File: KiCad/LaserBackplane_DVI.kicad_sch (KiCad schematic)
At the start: 48 parts, among them J1 Curr. Mod., J2 DVI-I, J5 Pz+, J6 Pz-, J7 Piezo_In, J8 Conn_Coaxial, K1 G6AU, Q1 MMBT3904, Q2 2N4401, U1 ADA4807-2ARM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

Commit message: Do not place the LED for assembly as this needs to match the frontpanel mounting hole (#15)
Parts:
- D4: Config (none) -> -PCBA
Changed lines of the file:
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@@
+			)
+		)
+		(property "Config" "-PCBA"
+			(at 165.1 41.91 90)
+			(effects
+				(font
+					(size 1.27 1.27)
+				)
+				(hide yes)
 			)
 		)

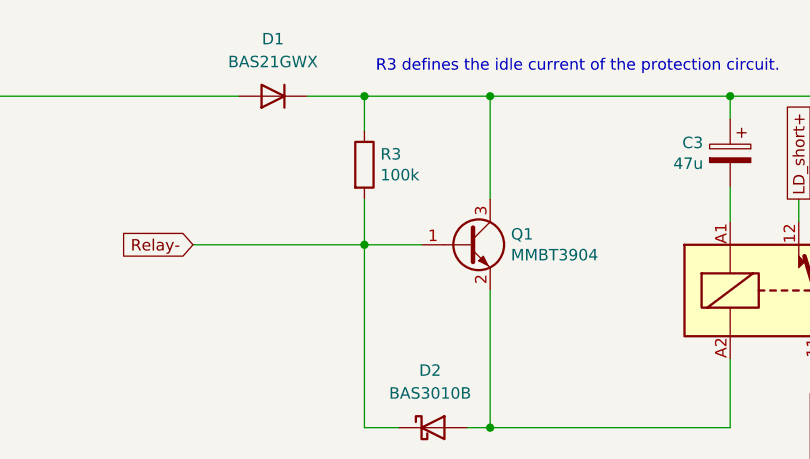
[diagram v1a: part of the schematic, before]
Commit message: Change R3 from 100k to 47k to increase the current through the relay during switch off
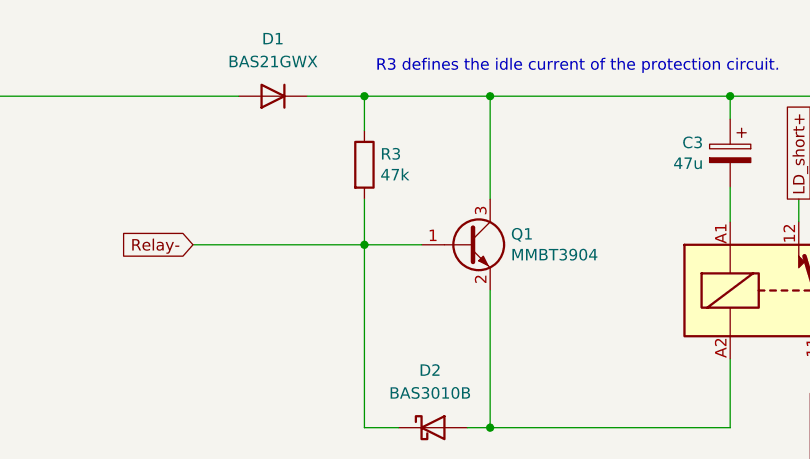
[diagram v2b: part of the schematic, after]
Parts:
- R3: value 100k -> 47k; PN CRCW0603100KFKEA -> CRCW060347K0FKEA
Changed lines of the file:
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@@
 			)
 		)
-		(property "Value" "100k"
+		(property "Value" "47k"
 			(at 85.598 32.893 0)
 			(effects
@@
 			)
 		)
-		(property "PN" "CRCW0603100KFKEA"
+		(property "PN" "CRCW060347K0FKEA"
 			(at 83.82 31.75 0)
 			(effects

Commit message: Bump to 1.8.1 (#17)
Updated authors
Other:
- company: Atoms-Photons-Quanta, Institut für Angewandte Physik, TU Darmstadt -> Atoms-Photons-Quanta, TU Darmstadt and Quantum Electronic Devices GmbH
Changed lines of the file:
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@@
 	(title_block
 		(title "Laser Backplane Diode DVI")
-		(date "2025-06-24")
-		(rev "1.8.0")
-		(company "Atoms-Photons-Quanta, Institut für Angewandte Physik, TU Darmstadt")
+		(date "2025-06-27")
+		(rev "1.8.1")
+		(company "Atoms-Photons-Quanta, TU Darmstadt and Quantum Electronic Devices GmbH")
 		(comment 1 "and Tilman Preuschoff")
-		(comment 2 "Copyright (©) 2024, Patrick Baus <patrick.baus@physik.tu-darmstadt.de>")
+		(comment 2 "Copyright (©) 2025, Patrick Baus <patrick.baus@quantum-electronic-devices.de>")
 	)
 	(text "R3 defines the idle current of the protection circuit."
@@
 	(symbol
 		(lib_id "Graphic:Logo_Open_Hardware_Small")
-		(at 275.59 173.99 0)
+		(at 279.4 176.53 0)
 		(unit 1)
 		(exclude_from_sim no)
@@
 		(dnp no)
 		(property "Reference" "LOGO2"
-			(at 275.59 167.005 0)
+			(at 279.4 169.545 0)
 			(effects
 				(font
@@
 		)
 		(property "Value" "Logo_Open_Hardware_Small"
-			(at 275.59 179.705 0)
+			(at 279.4 182.245 0)
 			(effects
 				(font
@@
 		)
 		(property "Footprint" "Symbol:OSHW-Logo_7.5x8mm_SilkScreen"
-			(at 275.59 173.99 0)
+			(at 279.4 176.53 0)
 			(effects
 				(font
@@
 		)
 		(property "Datasheet" "~"
-			(at 275.59 173.99 0)
+			(at 279.4 176.53 0)
 			(effects
 				(font
@@
 		)
 		(property "Description" "Open Hardware logo, small"
-			(at 275.59 173.99 0)
+			(at 279.4 176.53 0)
 			(effects
 				(font
@@
 		)
 		(property "MFN" ""
-			(at 275.59 173.99 0)
+			(at 279.4 176.53 0)
 			(effects
 				(font
@@
 		)
 		(property "PN" ""
-			(at 275.59 173.99 0)
+			(at 279.4 176.53 0)
 			(effects
 				(font

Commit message: Do not place the current mod SMA when using the PCBA service.
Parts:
- J1: Config +curr_mod -> +curr_mod,-PCBA
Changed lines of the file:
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@@
 			)
 		)
-		(property "Config" "+curr_mod"
+		(property "Config" "+curr_mod,-PCBA"
 			(at 25.4 161.29 0)
 			(effects

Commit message: Fixed product number of the relay. Removed dash before DC9 at the end.
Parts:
- K1: PN G6AU-274P-ST-US-DC9 -> G6AU-274P-ST-US DC9
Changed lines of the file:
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@@
 			)
 		)
-		(property "PN" "G6AU-274P-ST-US-DC9"
+		(property "PN" "G6AU-274P-ST-US DC9"
 			(at 134.62 45.72 0)
 			(effects

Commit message: Updared EEPROM symbol Enabled more ERC rules
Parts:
- U4: symbol Microchip:AT21CS11-STXXXX-X -> Microchip:AT21CS11-STU10‑T
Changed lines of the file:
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@@
 	)
 	(symbol
-		(lib_id "Microchip:AT21CS11-STXXXX-X")
+		(lib_id "Microchip:AT21CS11-STU10‑T")
 		(at 152.4 119.38 0)
 		(mirror y)
@@
 			)
 		)
-		(property "Description" "I2C Serial EEPROM, 1Kb (128x8) with Unique Serial Number, SOT-23"
+		(property "Description" "I2C Serial EEPROM, 1Kb (128x8) with Unique Serial Number, 2.7V to 4.5V, SOT-23"
 			(at 152.4 119.38 0)
 			(effects
